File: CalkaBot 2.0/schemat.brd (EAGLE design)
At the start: 100 x 100 mm, 65 parts, among them IC1 TB6612FNG, IC2 LM339D, IC3 7806DT, Q1 16MHz, X1 MINI-USB_4P-85-32004-40X

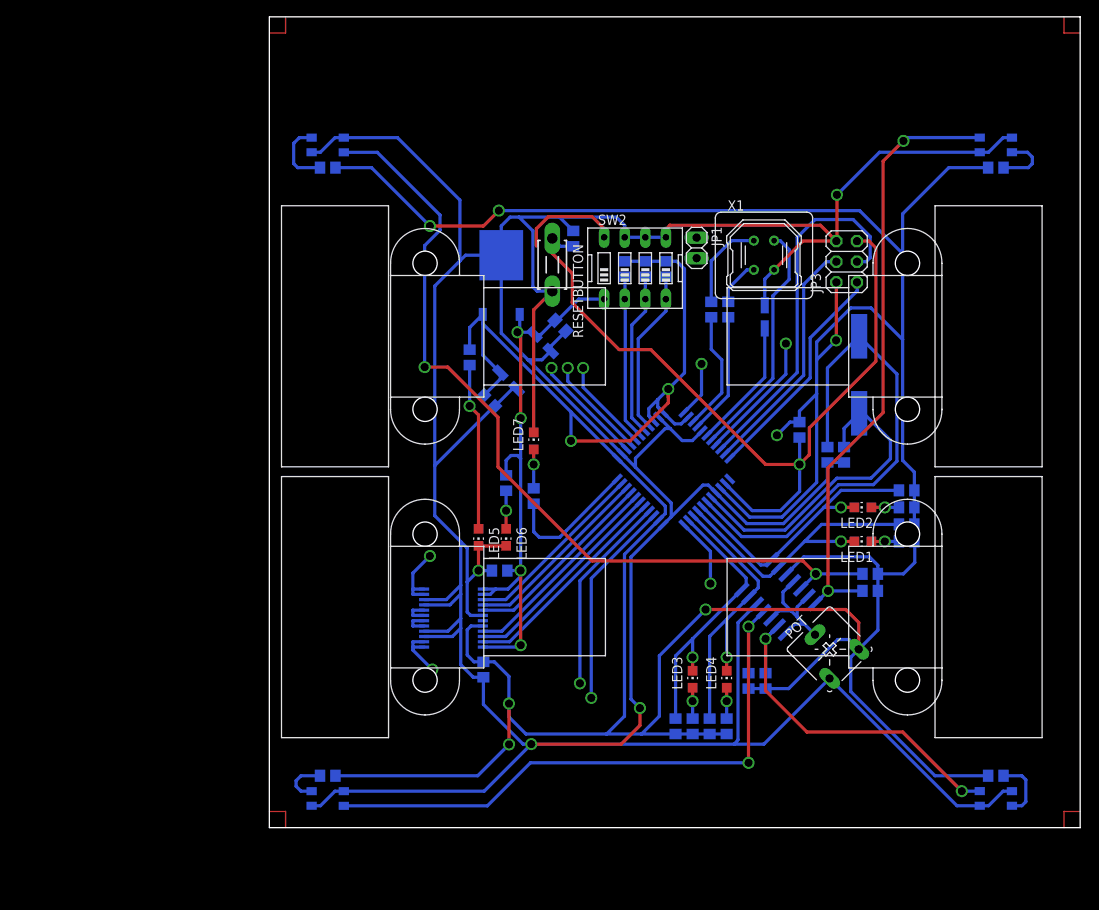
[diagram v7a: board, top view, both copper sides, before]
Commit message: przesunięte ścieżki i elementy żeby nie zasłaniały silniki
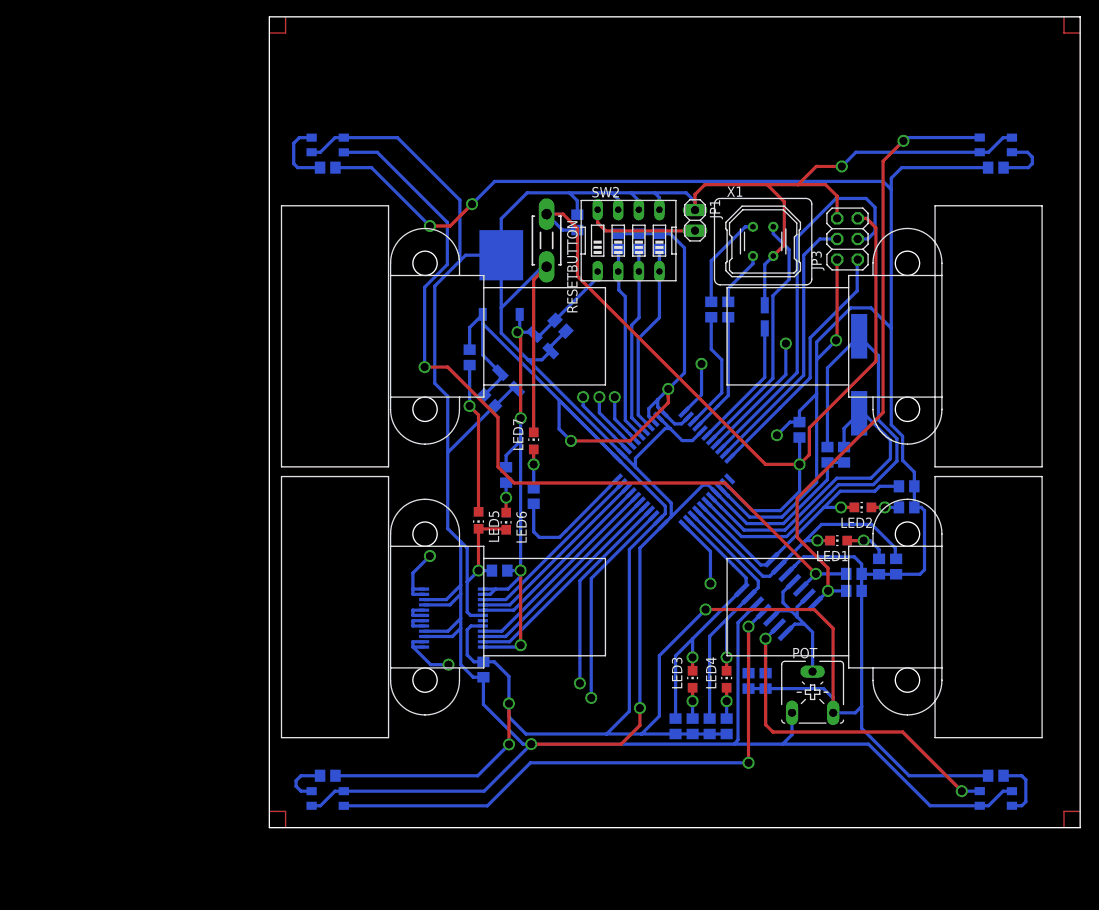
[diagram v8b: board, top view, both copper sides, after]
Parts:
- moved POT 5.70 mm to (67.0, 16.7), turned to 0 degrees
- moved R5 5.36 mm to (77.3, 32.2), turned to 270 degrees
- moved R18 4.60 mm to (75.2, 32.2), turned to 270 degrees
- moved SW2 3.49 mm to (44.3, 72.4)
- moved R2 3.49 mm to (48.1, 72.3)
- moved R6 3.49 mm to (45.6, 72.3)
- moved R9 3.49 mm to (43.0, 72.3)
- moved JP1 3.41 mm to (52.5, 74.9)
- moved RESETBUTTON 3.08 mm to (34.2, 72.4)
- moved LED1 3.00 mm to (70.2, 35.4)
- moved JP3 2.80 mm to (71.3, 72.6)
- moved LED5 2.10 mm to (25.8, 37.9)
- moved C3 2.06 mm to (38.0, 74.7)
- moved LED6 2.00 mm to (29.2, 37.8)
- moved R3 2.00 mm to (72.1, 31.3)
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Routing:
- net VCC: track 518.2 -> 548.1 mm
- net GND: track 535.8 -> 547.0 mm
- net POT: track 17.5 -> 26.9 mm
- net RST: track 99.7 -> 106.1 mm
- net I/O6: track 13.8 -> 8.63 mm
- net I/O5: track 12.7 -> 7.47 mm
- net I/O4: track 11.6 -> 6.35 mm
- net I/O3: track 20.5 -> 24.2 mm
- net MOSI: track 30.1 -> 33.5 mm
- net I/O1: track 20.4 -> 23.5 mm
- net I/O2: track 20.4 -> 23.5 mm
- net MISO: track 28.2 -> 31.0 mm
- net SCK: track 45.2 -> 47.6 mm
- net N$13: track 3.40 -> 5.56 mm
- net N$7: track 20.7 -> 18.6 mm
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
